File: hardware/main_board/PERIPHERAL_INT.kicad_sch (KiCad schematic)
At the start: 2 parts, among them J3 2x5 Socket Pins, J4 1x8 Male Pins

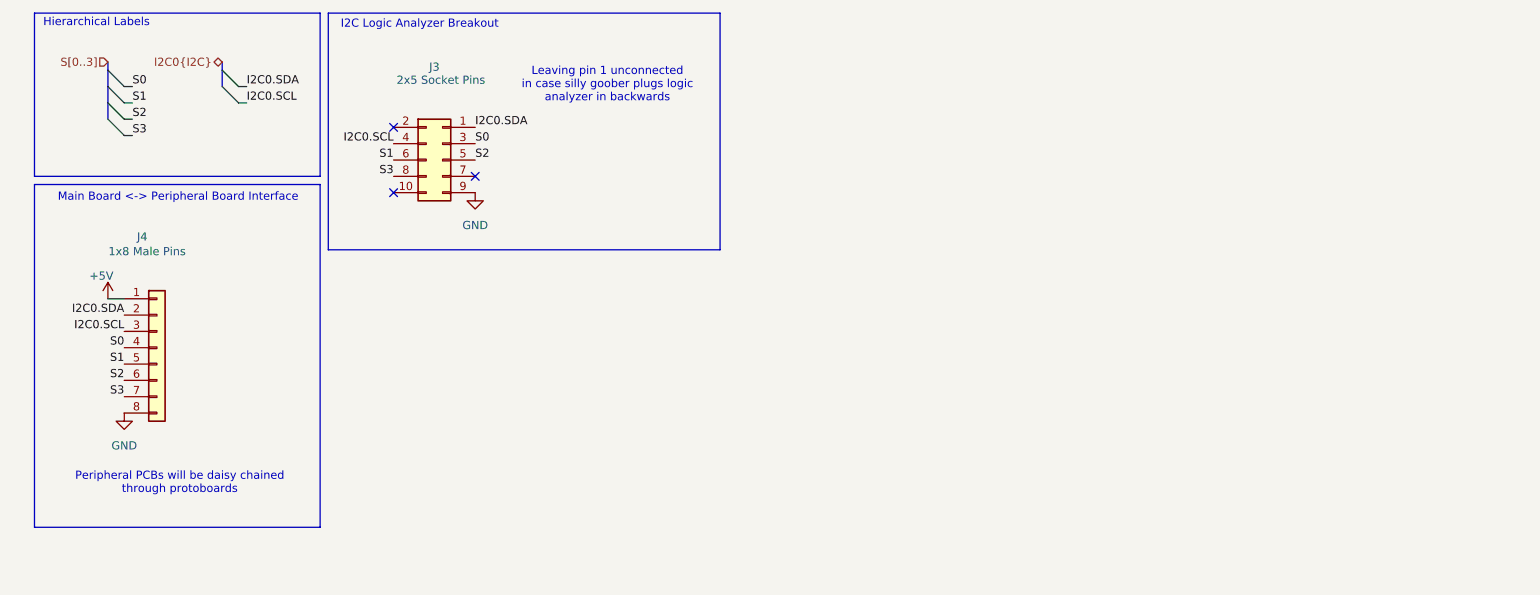
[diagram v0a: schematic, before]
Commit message: main board stuff. removed usbc for power. added level shifter for led logic signal. added lights for mux select signals. finished layout + pass DRC
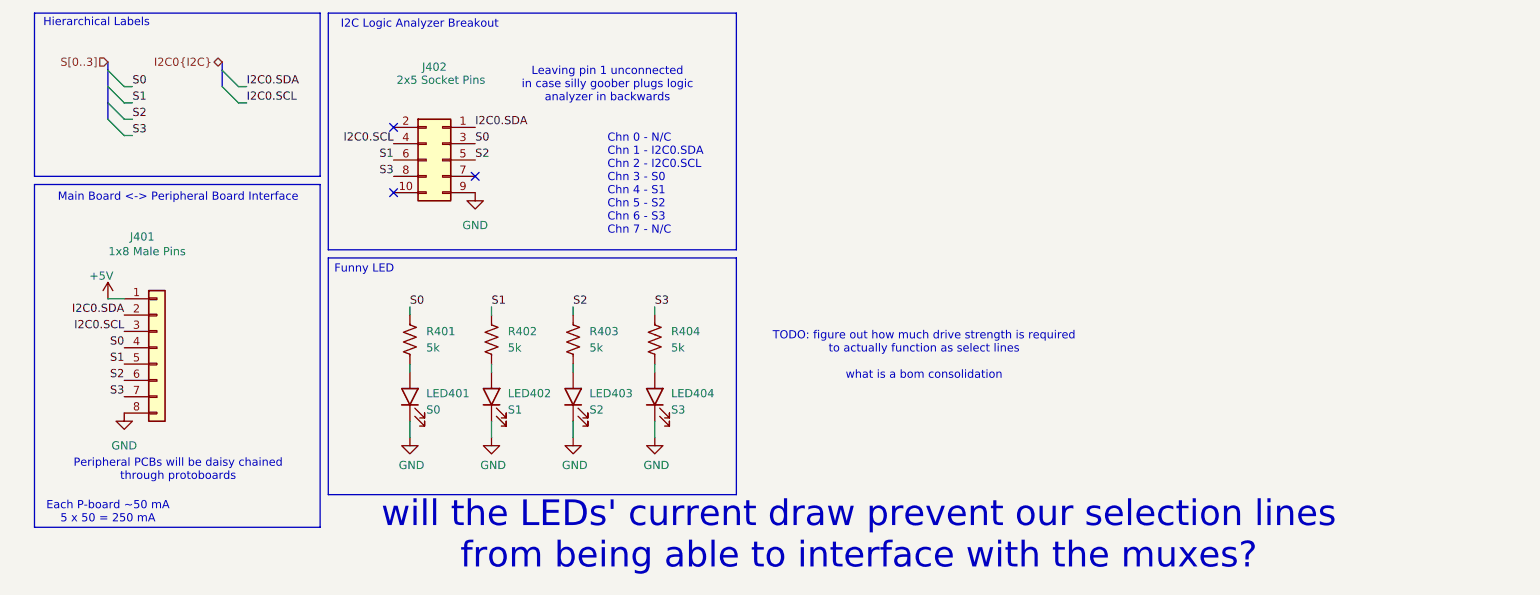
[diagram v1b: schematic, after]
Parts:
- added LED401: S0, SamacSys_Parts:LEDC2012X40N, symbol ECE445L:LED
- added LED402: S1, SamacSys_Parts:LEDC2012X40N, symbol ECE445L:LED
- added LED403: S2, SamacSys_Parts:LEDC2012X40N, symbol ECE445L:LED
- added LED404: S3, SamacSys_Parts:LEDC2012X40N, symbol ECE445L:LED
- added R401, R402, R403, R404: 5k, Resistor_SMD:R_0805_2012Metric, symbol Device:R_US
- renumbered J4 to J401, J3 to J402
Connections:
- net GND: now also LED401.1 (K), LED402.1 (K), LED403.1 (K), LED404.1 (K)
- net S0: now also R401.1
- net S1: now also R402.1
- net S2: now also R403.1
- net S3: now also R404.1
- new net: LED402.2 (A), R402.2
- new net: LED403.2 (A), R403.2
- new net: LED401.2 (A), R401.2
- new net: LED404.2 (A), R404.2
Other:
- note added: "Chn 0 - N/C Chn 1 - I2C0.SDA Chn 2 - I2C0.SCL Chn 3 - S0 Chn 4 - S1 Chn 5 - S2 Chn 6 - S3 Chn 7 - N/C"
- note added: "Each P-board ~50 mA 5 x 50 = 250 mA"
- note added: "Funny LED"
- note added: "TODO: figure out how much drive strength is required to actually function as select lines what is a bom consolidation"
- note added: "will the LEDs' current draw prevent our selection lines from being able to interface with the muxes?"

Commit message: bom
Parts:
- J401, J402: now left out of the parts list
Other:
- note added: "260 uA each -> 260 x 4 = 1.04 mA"
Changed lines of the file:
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@@
+		)
+	)
+	(text "260 uA each -> 260 x 4 = 1.04 mA"
+		(exclude_from_sim no)
+		(at 77.724 86.106 0)
+		(effects
+			(font
+				(size 1.27 1.27)
+			)
 		)
 	)
@@
 		(unit 1)
 		(exclude_from_sim no)
-		(in_bom yes)
+		(in_bom no)
 		(on_board yes)
 		(dnp no)
@@
 		(unit 1)
 		(exclude_from_sim no)
-		(in_bom yes)
+		(in_bom no)
 		(on_board yes)
 		(dnp no)

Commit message: changed level shifter. bunch of aesthetic changes. led resistors changed on main board. saving before nuke mouser.co.uk
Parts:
- R401, R402, R403, R404: value 5k -> 470
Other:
- note removed: "TODO: figure out how much drive strength is required to actually function as select lines what is a bom consolidation"
- note removed: "will the LEDs' current draw prevent our selection lines from being able to interface with the muxes?"
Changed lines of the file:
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@@
-		)
-	)
-	(text "TODO: figure out how much drive strength is required \nto actually function as select lines\n\nwhat is a bom consolidation"
-		(exclude_from_sim no)
-		(at 151.13 66.04 0)
-		(effects
-			(font
-				(size 1.27 1.27)
-			)
 		)
 	)
@@
 			(font
 				(size 1.27 1.27)
-			)
-		)
-	)
-	(text "will the LEDs' current draw prevent our selection lines\nfrom being able to interface with the muxes?"
-		(exclude_from_sim no)
-		(at 140.97 93.98 0)
-		(effects
-			(font
-				(size 4 4)
-				(color 255 13 0 1)
 			)
 		)
@@
 			)
 		)
-		(property "Value" "5k"
+		(property "Value" "470"
 			(at 111.76 64.7699 0)
 			(effects
@@
 			)
 		)
-		(property "Value" "5k"
+		(property "Value" "470"
 			(at 73.66 64.7699 0)
 			(effects
@@
 			)
 		)
-		(property "Value" "5k"
+		(property "Value" "470"
 			(at 86.36 64.7699 0)
 			(effects
@@
 			)
 		)
-		(property "Value" "5k"
+		(property "Value" "470"
 			(at 99.06 64.7699 0)
 			(effects

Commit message: finished everything except bom information. drc verification
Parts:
- LED401, LED402, LED403, LED404: Mouser Price/Stock https://www.mouser.co.uk/ProductDetail/ams-OSRAM/LS-R976-NR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 -> https://www.mouser.com/ProductDetail/ams-OSRAM/LS-R976-NR-1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
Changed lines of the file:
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@@
 			)
 		)
-		(property "Mouser Price/Stock" "https://www.mouser.co.uk/ProductDetail/ams-OSRAM/LS-R976-NR-1?qs=K5ta8V%252BWhtZhvCAe1sTZFg%3D%3D"
+		(property "Mouser Price/Stock" "https://www.mouser.com/ProductDetail/ams-OSRAM/LS-R976-NR-1?qs=K5ta8V%252BWhtZhvCAe1sTZFg%3D%3D"
 			(at 97.79 666.04 0)
 			(effects
@@
 			)
 		)
-		(property "Mouser Price/Stock" "https://www.mouser.co.uk/ProductDetail/ams-OSRAM/LS-R976-NR-1?qs=K5ta8V%252BWhtZhvCAe1sTZFg%3D%3D"
+		(property "Mouser Price/Stock" "https://www.mouser.com/ProductDetail/ams-OSRAM/LS-R976-NR-1?qs=K5ta8V%252BWhtZhvCAe1sTZFg%3D%3D"
 			(at 110.49 666.04 0)
 			(effects
@@
 			)
 		)
-		(property "Mouser Price/Stock" "https://www.mouser.co.uk/ProductDetail/ams-OSRAM/LS-R976-NR-1?qs=K5ta8V%252BWhtZhvCAe1sTZFg%3D%3D"
+		(property "Mouser Price/Stock" "https://www.mouser.com/ProductDetail/ams-OSRAM/LS-R976-NR-1?qs=K5ta8V%252BWhtZhvCAe1sTZFg%3D%3D"
 			(at 85.09 666.04 0)
 			(effects
@@
 			)
 		)
-		(property "Mouser Price/Stock" "https://www.mouser.co.uk/ProductDetail/ams-OSRAM/LS-R976-NR-1?qs=K5ta8V%252BWhtZhvCAe1sTZFg%3D%3D"
+		(property "Mouser Price/Stock" "https://www.mouser.com/ProductDetail/ams-OSRAM/LS-R976-NR-1?qs=K5ta8V%252BWhtZhvCAe1sTZFg%3D%3D"
 			(at 123.19 666.04 0)
 			(effects

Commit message: led info
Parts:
- LED401, LED402, LED403, LED404: Mouser Price/Stock https://www.mouser.com/ProductDetail/ams-OSRAM/LS-R976-NR-1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 -> https://www.mouser.com/ProductDetail/LITEON/LTST-C170GKT?qs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
- R401, R402, R403, R404: Mouser Price/Stock (none) -> https://www.mouser.com/ProductDetail/YAGEO/AF0805JR-07470RL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
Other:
- note added: "GRN"
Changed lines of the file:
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@@
+		)
+	)
+	(text "GRN"
+		(exclude_from_sim no)
+		(at 88.646 76.962 0)
+		(effects
+			(font
+				(size 1.27 1.27)
+			)
 		)
 	)
@@
 		)
 	)
+	(text "GRN"
+		(exclude_from_sim no)
+		(at 75.946 76.962 0)
+		(effects
+			(font
+				(size 1.27 1.27)
+			)
+		)
+	)
+	(text "GRN"
+		(exclude_from_sim no)
+		(at 113.792 76.962 0)
+		(effects
+			(font
+				(size 1.27 1.27)
+			)
+		)
+	)
 	(text "Peripheral PCBs will be daisy chained\nthrough protoboards"
 		(exclude_from_sim no)
@@
 		(exclude_from_sim no)
 		(at 35.052 41.402 0)
+		(effects
+			(font
+				(size 1.27 1.27)
+			)
+		)
+	)
+	(text "GRN"
+		(exclude_from_sim no)
+		(at 101.092 76.962 0)
 		(effects
 			(font
@@
 			)
 		)
-		(property "Datasheet" "https://datasheet.datasheetarchive.com/originals/distributors/DKDS-18/344792.pdf"
+		(property "Datasheet" ""
 			(at 97.79 266.04 0)
 			(effects
@@
 			)
 		)
-		(property "Mouser Price/Stock" "https://www.mouser.com/ProductDetail/ams-OSRAM/LS-R976-NR-1?qs=K5ta8V%252BWhtZhvCAe1sTZFg%3D%3D"
+		(property "Mouser Price/Stock" "https://www.mouser.com/ProductDetail/LITEON/LTST-C170GKT?qs=sGAEpiMZZMv0DJfhVcWlK%252BdbpgZMtcHOLj2jKamJQec%3D"
 			(at 97.79 666.04 0)
 			(effects
@@
 			)
 		)
-		(property "Datasheet" "https://datasheet.datasheetarchive.com/originals/distributors/DKDS-18/344792.pdf"
+		(property "Datasheet" ""
 			(at 110.49 266.04 0)
 			(effects
@@
 			)
 		)
-		(property "Mouser Price/Stock" "https://www.mouser.com/ProductDetail/ams-OSRAM/LS-R976-NR-1?qs=K5ta8V%252BWhtZhvCAe1sTZFg%3D%3D"
+		(property "Mouser Price/Stock" "https://www.mouser.com/ProductDetail/LITEON/LTST-C170GKT?qs=sGAEpiMZZMv0DJfhVcWlK%252BdbpgZMtcHOLj2jKamJQec%3D"
 			(at 110.49 666.04 0)
 			(effects
@@
 			)
 		)
-		(property "Datasheet" "https://datasheet.datasheetarchive.com/originals/distributors/DKDS-18/344792.pdf"
+		(property "Datasheet" ""
 			(at 85.09 266.04 0)
 			(effects
@@
 			)
 		)
-		(property "Mouser Price/Stock" "https://www.mouser.com/ProductDetail/ams-OSRAM/LS-R976-NR-1?qs=K5ta8V%252BWhtZhvCAe1sTZFg%3D%3D"
+		(property "Mouser Price/Stock" "https://www.mouser.com/ProductDetail/LITEON/LTST-C170GKT?qs=sGAEpiMZZMv0DJfhVcWlK%252BdbpgZMtcHOLj2jKamJQec%3D"
 			(at 85.09 666.04 0)
 			(effects
@@
 			)
 		)
+		(property "Mouser Price/Stock" "https://www.mouser.com/ProductDetail/YAGEO/AF0805JR-07470RL?qs=tggtontpCXOaQg0VhtuXeg%3D%3D"
+			(at 109.22 63.5 0)
+			(effects
+				(font
+					(size 1.27 1.27)
+				)
+				(hide yes)
+			)
+		)
 		(pin "1"
 		)
@@
 			)
 		)
+		(property "Mouser Price/Stock" "https://www.mouser.com/ProductDetail/YAGEO/AF0805JR-07470RL?qs=tggtontpCXOaQg0VhtuXeg%3D%3D"
+			(at 71.12 63.5 0)
+			(effects
+				(font
+					(size 1.27 1.27)
+				)
+				(hide yes)
+			)
+		)
 		(pin "1"
 		)
@@
 			)
 		)
-		(property "Datasheet" "https://datasheet.datasheetarchive.com/originals/distributors/DKDS-18/344792.pdf"
+		(property "Datasheet" ""
 			(at 123.19 266.04 0)
 			(effects
@@
 			)
 		)
-		(property "Mouser Price/Stock" "https://www.mouser.com/ProductDetail/ams-OSRAM/LS-R976-NR-1?qs=K5ta8V%252BWhtZhvCAe1sTZFg%3D%3D"
+		(property "Mouser Price/Stock" "https://www.mouser.com/ProductDetail/LITEON/LTST-C170GKT?qs=sGAEpiMZZMv0DJfhVcWlK%252BdbpgZMtcHOLj2jKamJQec%3D"
 			(at 123.19 666.04 0)
 			(effects
@@
 			)
 		)
+		(property "Mouser Price/Stock" "https://www.mouser.com/ProductDetail/YAGEO/AF0805JR-07470RL?qs=tggtontpCXOaQg0VhtuXeg%3D%3D"
+			(at 83.82 63.5 0)
+			(effects
+				(font
+					(size 1.27 1.27)
+				)
+				(hide yes)
+			)
+		)
 		(pin "1"
 		)
@@
 			(at 96.52 63.5 0)
 			(effects
+				(font
+					(size 1.27 1.27)
+				)
+				(hide yes)
+			)
+		)
+		(property "Mouser Price/Stock" "https://www.mouser.com/ProductDetail/YAGEO/AF0805JR-07470RL?qs=tggtontpCXOaQg0VhtuXeg%3D%3D"
+			(at 96.52 63.5 0)
+			(effects
